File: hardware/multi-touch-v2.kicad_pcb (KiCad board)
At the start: 2 copper layers, 25 x 30 mm, 28 parts, among them P1 CON-SENSOR2, P2 DEBUG, P3 BOOT, P4 CONN_01X12, U1 CPT112S, U2 XMC1XXX24, U3 DRILL, U4 DRILL, U5 DRILL, U6 DRILL

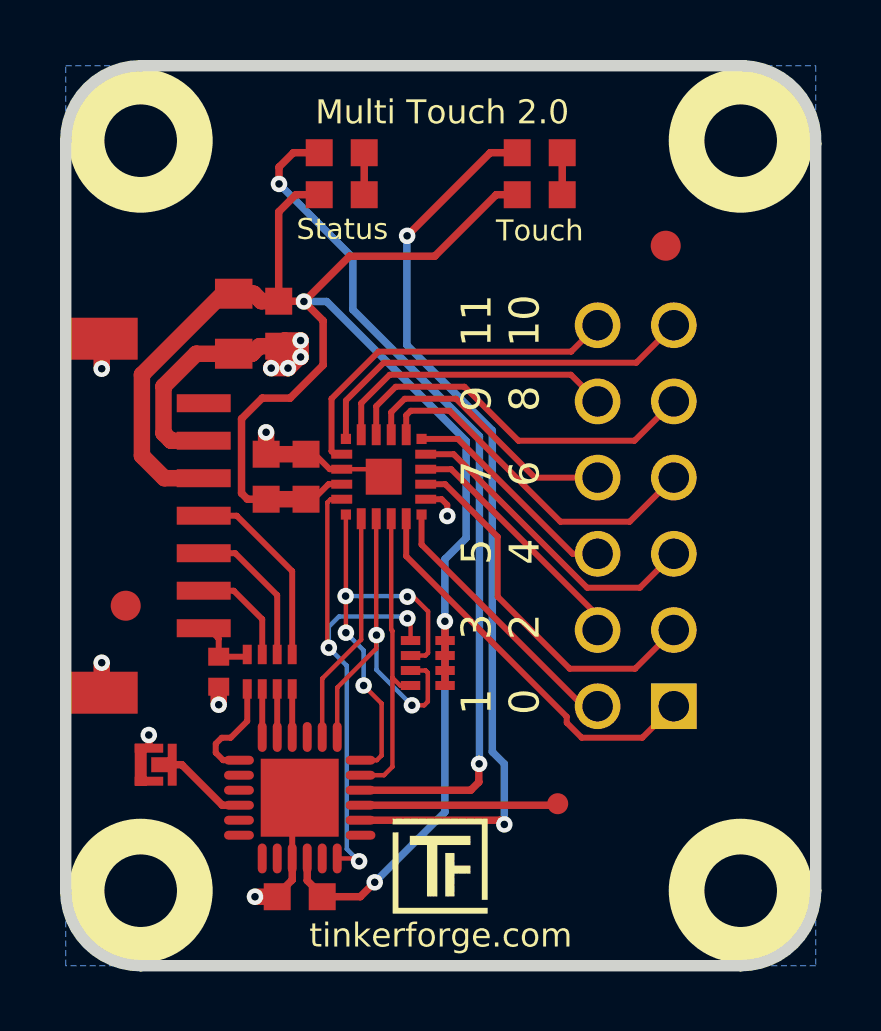
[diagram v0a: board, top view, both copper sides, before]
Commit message: changed touch controller to MPR121Q
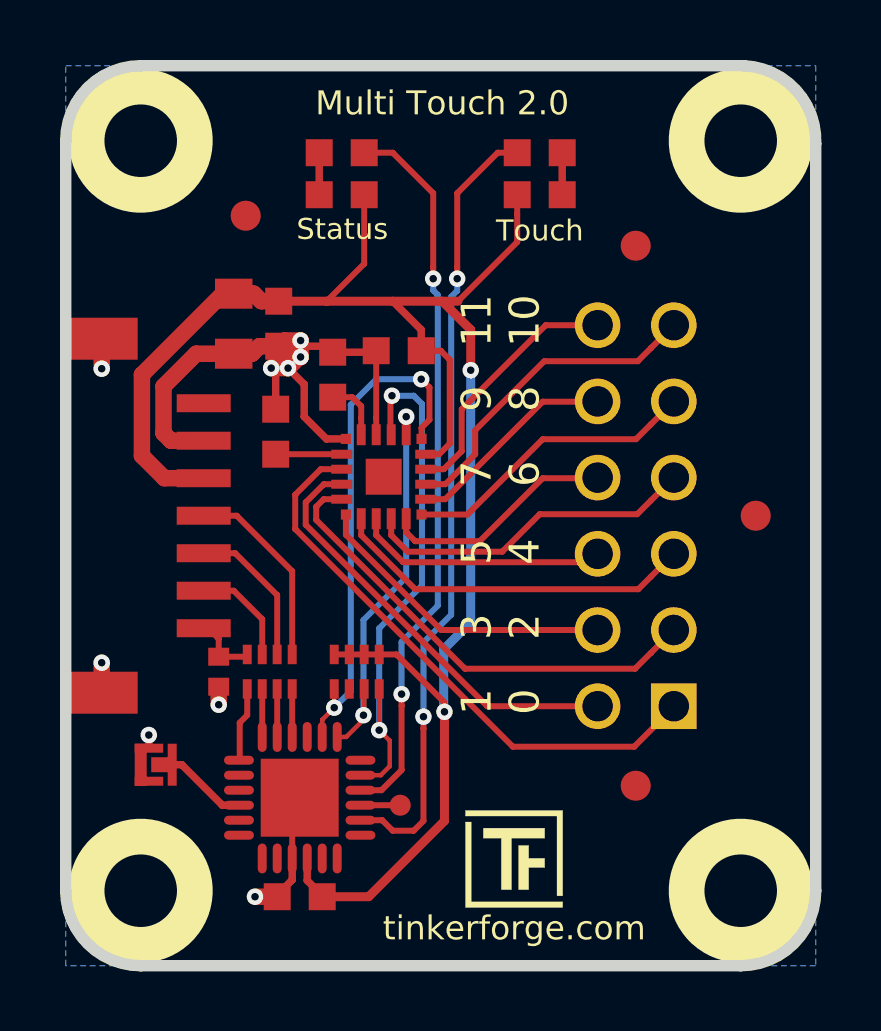
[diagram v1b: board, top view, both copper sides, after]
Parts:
- removed the Fiducial_Mark at (62.9, 33.3)
- removed the Fiducial_Mark at (44.9, 45.3)
- removed the G*** at (53.8, 52.4)
- removed the G*** at (55.4, 34.8)
- removed the VAL at (55.4, 42.3)
- removed the VAL at (55.4, 49.8)
- added Fiducial_Mark: VAL**, tinkerforge:Fiducial_Mark, F.Cu at (48.9, 32.3)
- added Fiducial_Mark: VAL**, tinkerforge:Fiducial_Mark, F.Cu at (61.9, 33.3)
- added Fiducial_Mark: VAL**, tinkerforge:Fiducial_Mark, F.Cu at (61.9, 51.3)
- added Fiducial_Mark: VAL**, tinkerforge:Fiducial_Mark, F.Cu at (65.9, 42.3)
- added G***: LOGO, tinkerforge:Logo_31x31, F.Cu at (57.9, 53.8)
- added G***: LOGO, tinkerforge:Logo_CoMCU, B.Cu at (55.4, 35.6)
- added R2: 75k, tinkerforge:R0603F, F.Cu at (49.9, 39.5)
- added VAL: WEEE_7mm, tinkerforge:WEEE_7mm, B.Cu at (55.4, 42.3)
- added VAL: CE_5mm, tinkerforge:CE_5mm, B.Cu at (55.4, 48.5)
- C1: value 4u7 -> 100nF; footprint kicad-libraries:C0603F -> tinkerforge:C0603F
- RP2: value TBD (2k2) -> 10k
- U1: value CPT112S -> MPR121Q; footprint kicad-libraries:QFN-20-3x3 -> tinkerforge:QFN-20-3x3
- U2: value XMC1XXX24 -> XMC1100
- moved C6 6.10 mm to (54.0, 36.8), turned to 0 degrees
- moved P2 5.25 mm to (54.0, 52.0)
- moved C1 3.51 mm to (51.8, 37.6), turned to 90 degrees
- moved RP2 2.39 mm to (52.6, 47.5), turned to 180 degrees
- turned D2 to 180 degrees
- turned R5 to 180 degrees
- turned U1 to 270 degrees
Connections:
- C1 pad 1: GND -> Net-(C1-Pad1)
- C1 pad 2: VCC -> GND
- P1 pad 1: Net-(P1-Pad1) -> (no net)
- RP2 pad 5: SCL_Conf -> INT
- RP2 pad 6: SDA-Conf -> (no net)
- U1 pad 1: Net-(P4-Pad11) -> INT
- U1 pad 10: Net-(P4-Pad1) -> Net-(P4-Pad3)
- U1 pad 11: Net-(P4-Pad2) -> Net-(P4-Pad4)
- U1 pad 12: GND -> Net-(P4-Pad5)
- U1 pad 13: Net-(P4-Pad3) -> Net-(P4-Pad6)
- U1 pad 14: Net-(P4-Pad4) -> Net-(P4-Pad7)
- U1 pad 15: Net-(P4-Pad5) -> Net-(P4-Pad8)
- U1 pad 16: Net-(P4-Pad6) -> Net-(P4-Pad9)
- U1 pad 17: Net-(P4-Pad7) -> Net-(P4-Pad10)
- U1 pad 18: Net-(P4-Pad8) -> Net-(P4-Pad11)
- U1 pad 19: Net-(P4-Pad9) -> Net-(P4-Pad12)
- U1 pad 2: Net-(P4-Pad12) -> SCL
- U1 pad 20: Net-(P4-Pad10) -> VCC
- U1 pad 3: GND -> SDA
- U1 pad 4: VCC -> GND
- U1 pad 5: SCL_Conf -> Net-(C1-Pad1)
- U1 pad 6: SDA-Conf -> GND
- U1 pad 7: INT -> Net-(R2-Pad1)
- U1 pad 8: SCL -> Net-(P4-Pad1)
- U1 pad 9: SDA -> Net-(P4-Pad2)
- U1 pad EP: GND -> (no net)
- U2 pad 11: Net-(U2-Pad11) -> (no net)
- U2 pad 12: SCL_Conf -> (no net)
- U2 pad 13: Net-(U2-Pad13) -> (no net)
- U2 pad 18: SDA-Conf -> (no net)
- U2 pad 2: Net-(U2-Pad2) -> (no net)
- U2 pad 21: Net-(U2-Pad21) -> (no net)
- U2 pad 3: Net-(U2-Pad3) -> (no net)
- U2 pad 5: Net-(U2-Pad5) -> (no net)
- U2 pad 6: Net-(U2-Pad6) -> (no net)
- U2 pad 7: Net-(U2-Pad7) -> (no net)
- U2 pad 8: Net-(U2-Pad8) -> (no net)
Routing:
- net SCL_Conf: track 18.0 -> 0.00 mm, vias 3 -> 0
- net SDA-Conf: track 14.3 -> 0.00 mm, vias 4 -> 0
- net INT: track 7.81 -> 17.0 mm, vias 0 -> 2
- net SDA: track 10.2 -> 17.7 mm, vias 0 -> 2
- net GND: track 33.1 -> 39.4 mm, vias 11 -> 9
- net Net-(P4-Pad1): track 13.2 -> 19.2 mm
- net Net-(P4-Pad2): track 9.10 -> 14.4 mm
- net Net-(P2-Pad1): track 6.60 -> 1.32 mm
- net Net-(R5-Pad1): track 28.9 -> 24.3 mm
- net Net-(R1-Pad1): track 30.6 -> 26.3 mm
- net Net-(P4-Pad12): track 12.0 -> 8.54 mm
- net VCC: track 65.8 -> 62.3 mm, vias 3 -> 2
- net Net-(P4-Pad3): track 12.5 -> 15.9 mm
- net Net-(P4-Pad10): track 9.69 -> 7.08 mm
- net Net-(P4-Pad9): track 12.4 -> 9.97 mm
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
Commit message: changed footprint of MPR121Q from QFN-20-3x3 to QFN20-3x3
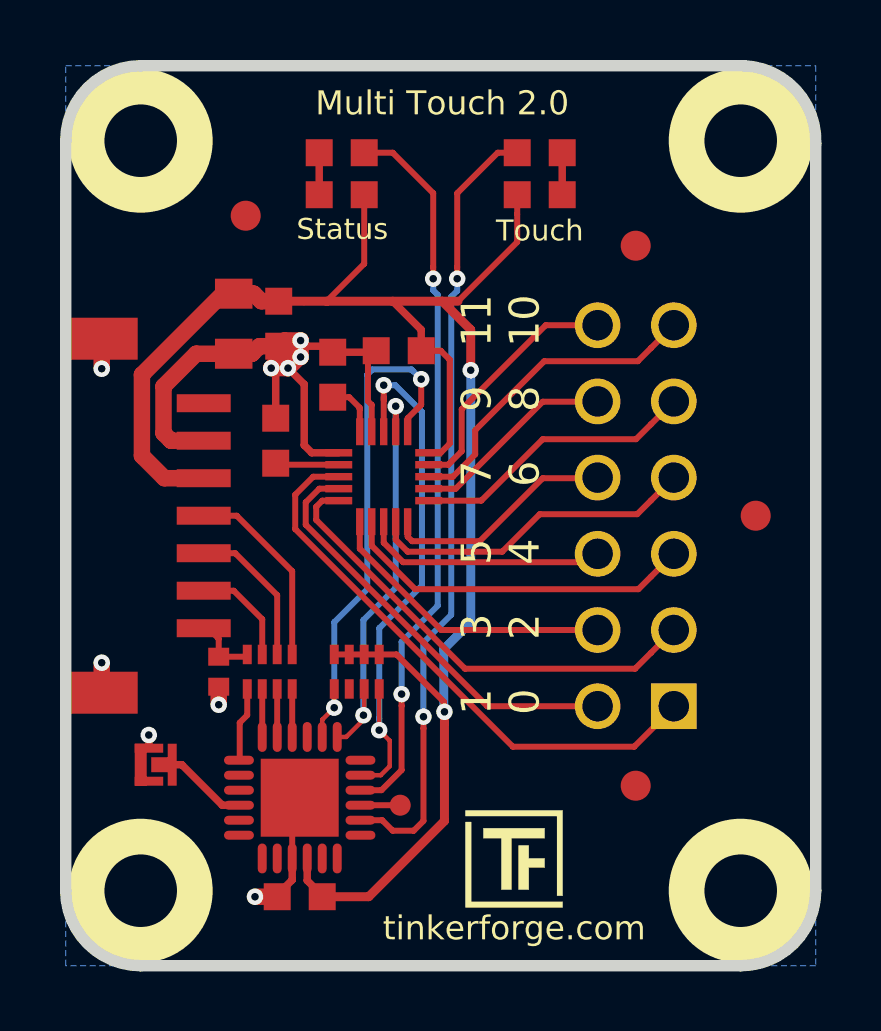
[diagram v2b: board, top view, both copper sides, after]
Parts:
- U1: footprint tinkerforge:QFN-20-3x3 -> tinkerforge:QFN20-3X3
- moved R2 0.30 mm to (49.9, 39.8)
- turned U1 to 180 degrees
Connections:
- P1 pad 1: (no net) -> Net-(P1-Pad1)
- RP2 pad 6: (no net) -> Net-(RP2-Pad6)
- U2 pad 11: (no net) -> Net-(U2-Pad11)
- U2 pad 12: (no net) -> Net-(U2-Pad12)
- U2 pad 13: (no net) -> Net-(U2-Pad13)
- U2 pad 18: (no net) -> Net-(U2-Pad18)
- U2 pad 2: (no net) -> Net-(U2-Pad2)
- U2 pad 21: (no net) -> Net-(U2-Pad21)
- U2 pad 3: (no net) -> Net-(U2-Pad3)
- U2 pad 5: (no net) -> Net-(U2-Pad5)
- U2 pad 6: (no net) -> Net-(U2-Pad6)
- U2 pad 7: (no net) -> Net-(U2-Pad7)
- U2 pad 8: (no net) -> Net-(U2-Pad8)
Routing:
- net SDA: track 17.7 -> 18.4 mm
- net GND: track 39.4 -> 40.1 mm

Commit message: drc
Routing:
- net INT: track 17.3 -> 18.1 mm
- net Net-(R5-Pad1): track 24.3 -> 25.0 mm
- net SCL: track 13.5 -> 14.0 mm
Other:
- net class Default: clearance 0.15 -> 0.149
- rule trace_clearance: 0.15 -> 0.149

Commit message: changed "touch" led from blue to green
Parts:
- D1: value blue -> green
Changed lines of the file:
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@@
   )
   (layers
-    (0 Vorderseite power)
-    (31 Rückseite signal)
-    (32 B.Adhes user)
-    (33 F.Adhes user)
-    (34 B.Paste user)
-    (35 F.Paste user)
-    (36 B.SilkS user)
+    (0 Vorderseite power hide)
+    (31 Rückseite signal hide)
+    (32 B.Adhes user hide)
+    (33 F.Adhes user hide)
+    (34 B.Paste user hide)
+    (35 F.Paste user hide)
+    (36 B.SilkS user hide)
     (37 F.SilkS user)
-    (38 B.Mask user)
-    (39 F.Mask user)
+    (38 B.Mask user hide)
+    (39 F.Mask user hide)
     (40 Dwgs.User user)
     (41 Cmts.User user)
@@
     (visible_elements FFFFFFBF)
     (pcbplotparams
-      (layerselection 0x010fc_80000001)
+      (layerselection 0x010fc_ffffffff)
       (usegerberextensions true)
       (usegerberattributes false)
@@
       (drillshape 0)
       (scaleselection 1)
-      (outputdirectory "/tmp/multi/"))
+      (outputdirectory "proto/"))
   )
   (net 0 "")
@@
       (effects (font (size 0.2 0.2) (thickness 0.05)))
     )
-    (fp_text value blue (at 0.75 0.45) (layer F.Fab)
-      (effects (font (size 0.2 0.2) (thickness 0.05)))
-    )
+    (fp_text value green (at 0.75 0.45) (layer F.Fab)
+      (effects (font (size 0.2 0.2) (thickness 0.05)))
+    )
